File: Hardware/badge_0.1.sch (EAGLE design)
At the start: 59 parts, among them CON1 PH_2, IC1 CP2102, SW2 MK12C02, U1 SMBT2222A, U2 SMBT2222A, U4 MCP73832T-2DCI/OT

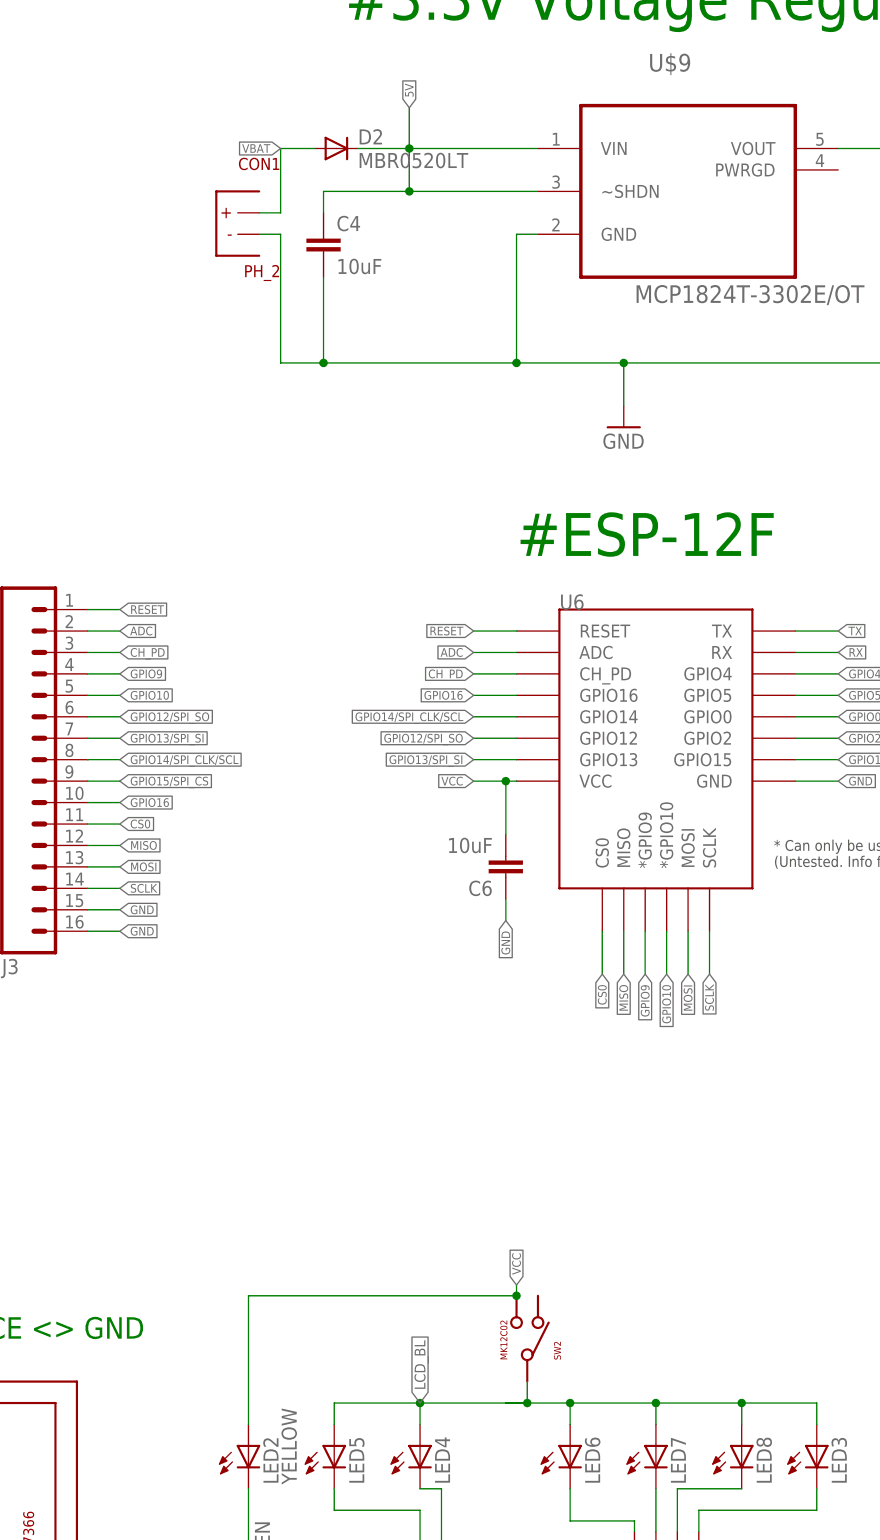
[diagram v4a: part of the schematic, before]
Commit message: Added optional connections to the anchors for the battery connector and slide switch To place on schematic, use the invoke tool
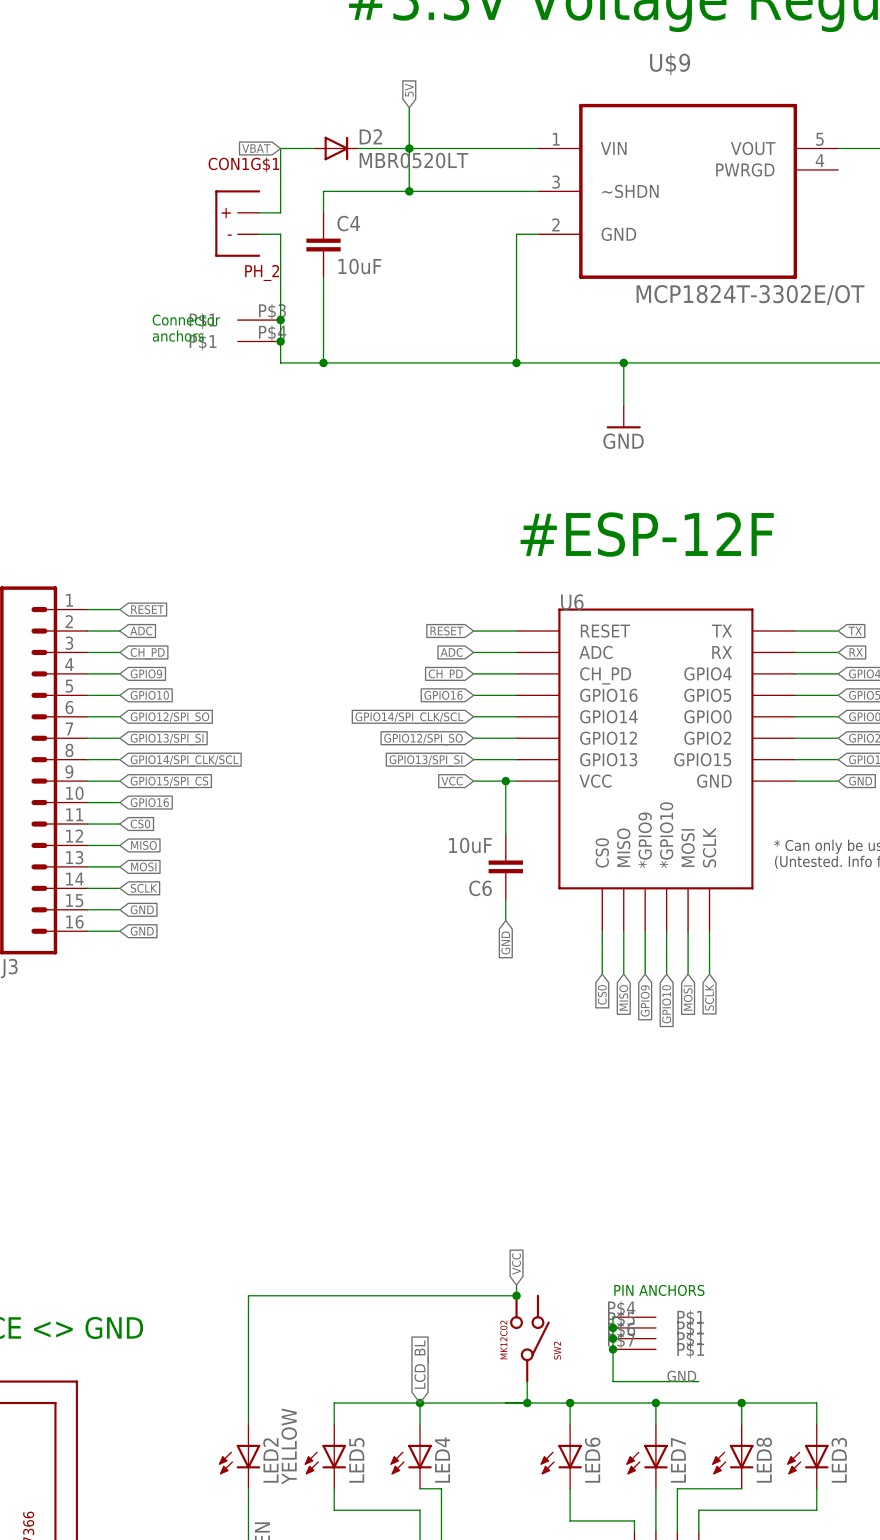
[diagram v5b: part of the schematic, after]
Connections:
- net GND: now also CON1ANCH1.P$1, CON1ANCH2.P$1, CON1G$1.P$2, SW2G$2.P$1, SW2G$3.P$1, SW2G$4.P$1, SW2G$5.P$1; no longer CON1.P$2
- net LCD_BL: now also SW2G$1.P$1; no longer SW2.P$1
- net VBAT: now also CON1G$1.P$1; no longer CON1.P$1
- net VCC: now also SW2G$1.P$3; no longer SW2.P$3
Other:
- note added: "Connector anchors"
- note added: "PIN ANCHORS"
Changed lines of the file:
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@@
 <?xml version="1.0" encoding="utf-8"?>
 <!DOCTYPE eagle SYSTEM "eagle.dtd">
-<eagle version="7.5.0">
+<eagle version="7.1.0">
 <drawing>
 <settings>
@@
 for USB-Serial functionalities</text>
 <text x="182.88" y="83.82" size="2.54" layer="91">CHECK /SCE &lt;&gt; GND</text>
+<text x="217.17" y="201.93" size="1.27" layer="91" font="vector">Connector
+anchors</text>
+<text x="271.78" y="88.9" size="1.27" layer="91" font="vector">PIN ANCHORS</text>
 </plain>
 <instances>
@@
 <instance part="LED2" gate="G$1" x="228.6" y="71.12"/>
 <instance part="C1" gate="G$1" x="43.18" y="118.11"/>
-<instance part="CON1" gate="G$1" x="224.79" y="214.63" rot="MR0"/>
+<instance part="CON1" gate="G$1" x="224.79" y="214.63" smashed="yes" rot="MR0">
+<attribute name="NAME" x="232.41" y="222.25" size="1.4224" layer="94" rot="MR0"/>
+<attribute name="VALUE" x="232.41" y="209.55" size="1.4224" layer="94" rot="MR0"/>
+</instance>
 <instance part="IC1" gate="G$1" x="81.28" y="213.36"/>
 <instance part="J2" gate="G$1" x="132.08" y="208.28" rot="R180"/>
@@
 <instance part="D2" gate="G$1" x="239.014" y="224.79"/>
 <instance part="C2" gate="G$1" x="316.23" y="214.63"/>
+<instance part="CON1" gate="ANCH1" x="227.33" y="204.47" smashed="yes" rot="R180"/>
+<instance part="CON1" gate="ANCH2" x="227.33" y="201.93" smashed="yes" rot="R180"/>
+<instance part="SW2" gate="G$2" x="276.86" y="86.36"/>
+<instance part="SW2" gate="G$3" x="276.86" y="85.09"/>
+<instance part="SW2" gate="G$5" x="276.86" y="82.55"/>
+<instance part="SW2" gate="G$4" x="276.86" y="83.82"/>
 </instances>
 <busses>
@@
 <pinref part="CON1" gate="G$1" pin="P$2"/>
 <wire x1="229.87" y1="214.63" x2="232.41" y2="214.63" width="0.1524" layer="91"/>
-<wire x1="232.41" y1="214.63" x2="232.41" y2="199.39" width="0.1524" layer="91"/>
+<wire x1="232.41" y1="214.63" x2="232.41" y2="204.47" width="0.1524" layer="91"/>
 <pinref part="C2" gate="G$1" pin="2"/>
+<wire x1="232.41" y1="204.47" x2="232.41" y2="201.93" width="0.1524" layer="91"/>
+<wire x1="232.41" y1="201.93" x2="232.41" y2="199.39" width="0.1524" layer="91"/>
 <wire x1="306.07" y1="199.39" x2="316.23" y2="199.39" width="0.1524" layer="91"/>
 <wire x1="316.23" y1="199.39" x2="316.23" y2="212.09" width="0.1524" layer="91"/>
 <junction x="306.07" y="199.39"/>
+<pinref part="CON1" gate="ANCH1" pin="P$1"/>
+<junction x="232.41" y="204.47"/>
+<pinref part="CON1" gate="ANCH2" pin="P$1"/>
+<junction x="232.41" y="201.93"/>
 </segment>
 <segment>
@@
 <junction x="180.34" y="68.58"/>
 </segment>
+<segment>
+<pinref part="SW2" gate="G$2" pin="P$1"/>
+<pinref part="SW2" gate="G$3" pin="P$1"/>
+<wire x1="271.78" y1="86.36" x2="271.78" y2="85.09" width="0.1524" layer="91"/>
+<pinref part="SW2" gate="G$4" pin="P$1"/>
+<wire x1="271.78" y1="85.09" x2="271.78" y2="83.82" width="0.1524" layer="91"/>
+<junction x="271.78" y="85.09"/>
+<pinref part="SW2" gate="G$5" pin="P$1"/>
+<wire x1="271.78" y1="83.82" x2="271.78" y2="82.55" width="0.1524" layer="91"/>
+<junction x="271.78" y="83.82"/>
+<wire x1="271.78" y1="82.55" x2="271.78" y2="78.74" width="0.1524" layer="91"/>
+<junction x="271.78" y="82.55"/>
+<wire x1="271.78" y1="78.74" x2="281.94" y2="78.74" width="0.1524" layer="91"/>
+<label x="278.13" y="78.74" size="1.27" layer="95" font="vector"/>
+</segment>
 </net>
